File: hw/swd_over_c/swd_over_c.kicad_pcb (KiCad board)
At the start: 4 copper layers, 18.5 x 16 mm, 17 parts, among them J1 USB-C Receptacle, J2 Conn_ARM_JTAG_SWD_10, P1 USB_C_Plug, U1 ATtiny24-20M

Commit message: v1.5
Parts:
- P1: footprint alvarop:MOLEX_1054440011 -> alvarop:MOLEX_1054440011_PCBWAY
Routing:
- net GND: track 20.6 -> 20.1 mm
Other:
- board text added: "v1.5"
- board text removed: "v1.4"

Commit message: v1.6 changes
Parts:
- J1: value USB-C Receptacle -> USB_C_Receptacle_USB2.0
- P1: footprint alvarop:MOLEX_1054440011_PCBWAY -> alvarop:‎USB4155-03-C‎
- moved REF** 0.50 mm to (176.6, 67.6)
- moved P1 0.07 mm to (180.0, 67.5), turned to 90 degrees
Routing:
- net /NRST: track 15.6 -> 13.6 mm
- net /D-: track 24.3 -> 22.2 mm
- net /CC1: track 11.7 -> 9.65 mm
- net /SBU1: track 16.1 -> 14.1 mm
- net /D+: track 25.8 -> 23.8 mm
- net /SWO: track 14.3 -> 12.3 mm
- net /SHIELD: track 19.5 -> 17.9 mm
- net GND: track 20.1 -> 18.6 mm, vias 12 -> 14
- net /SBU2: track 16.2 -> 15.8 mm, vias 1 -> 2
- net /SWDCLK: track 14.0 -> 13.7 mm, vias 0 -> 1
- net /SWDIO: track 14.1 -> 13.8 mm, vias 0 -> 1
- net VBUS: track 8.53 -> 8.37 mm, vias 5 -> 7
- net /CC2: track 12.5 -> 12.6 mm, vias 1 -> 2
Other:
- board size 18.5 x 16 mm -> 25 x 16 mm
- board text added: "v1.6"
- board text removed: "v1.5"

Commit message: Somehow got the values for R4 and R5 swapped...
Swapped them in schematic and in code (manually reworked v1.6 boards to swap R4/R5)
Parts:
- R4: value 56k -> 10k
- R5: value 10k -> 56k
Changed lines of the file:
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@@
   (title_block
     (title "Debugotron - SWD to USB-C")
-    (date "2022-05-15")
-    (rev "1.6")
+    (date "2022-06-07")
+    (rev "1.7")
     (company "Quesadillon LLC")
   )
@@
     (descr "Resistor SMD 0402 (1005 Metric), square (rectangular) end terminal, IPC_7351 nominal, (Body size source: IPC-SM-782 page 72, https://www.pcb-3d.com/wordpress/wp-content/uploads/ipc-sm-782a_amendment_1_and_2.pdf), generated with kicad-footprint-generator")
     (tags "resistor")
-    (property "Description" "RES 56K OHM 1% 1/16W 0402")
+    (property "Description" "RES 10K OHM 1% 1/16W 0402")
     (property "Footprint(Generic)" "R0402")
-    (property "MPN" "RC0402FR-0756KL")
+    (property "MPN" "RC0402FR-0710KL")
     (property "Manufacturer" "Yageo")
     (property "Sheetfile" "swd_over_c.kicad_sch")
     (property "Sheetname" "")
     (property "Vendor" "Digi-Key")
-    (property "Vendor Part Number" "311-56.0KLRCT-ND")
+    (property "Vendor Part Number" "311-10.0KLRCT-ND")
     (attr smd)
     (fp_text reference "R4" (at 0 -1.17) (layer "F.SilkS") hide
       (effects (font (size 1 1) (thickness 0.15)))
     )
-    (fp_text value "56k" (at -2.074995 0.30001) (layer "F.Fab") hide
+    (fp_text value "10k" (at -2.074995 0.30001) (layer "F.Fab") hide
       (effects (font (size 1 1) (thickness 0.15)))
     )
@@
   (footprint "alvarop:‎USB4155-03-C‎" (layer "F.Cu")
     (at 179.999996 67.499992 90)
-    (property "Description" "CONN PLUG USB3.1 TYPEC BRD EDGE")
-    (property "Footprint(Generic)" "1054440011")
-    (property "MPN" "1054440011")
-    (property "Manufacturer" "Molex")
-    (property "Sheetfile" "swd_over_c.kicad_sch")
-    (property "Sheetname" "")
-    (property "Vendor" "Digi-Key")
-    (property "Vendor Part Number" "900-1054440011CT-ND")
+    (property "Description" "USB TYPE C, PLUG, SMT , G/F, RIG")
+    (property "Footprint(Generic)" "USB4155-03-C")
+    (property "MPN" "USB4155-03-C")
+    (property "Manufacturer" "GCT")
+    (property "Sheetfile" "swd_over_c.kicad_sch")
+    (property "Sheetname" "")
+    (property "Vendor" "Digi-Key")
+    (property "Vendor Part Number" "2073-USB4155-03-CCT-ND")
     (attr smd)
     (fp_text reference "P1" (at 0.125 -4.8 90 unlocked) (layer "F.SilkS") hide
@@
     (descr "Resistor SMD 0402 (1005 Metric), square (rectangular) end terminal, IPC_7351 nominal, (Body size source: IPC-SM-782 page 72, https://www.pcb-3d.com/wordpress/wp-content/uploads/ipc-sm-782a_amendment_1_and_2.pdf), generated with kicad-footprint-generator")
     (tags "resistor")
-    (property "Description" "RES 10K OHM 1% 1/16W 0402")
+    (property "Description" "RES 56K OHM 1% 1/16W 0402")
     (property "Footprint(Generic)" "R0402")
-    (property "MPN" "RC0402FR-0710KL")
+    (property "MPN" "RC0402FR-0756KL")
     (property "Manufacturer" "Yageo")
     (property "Sheetfile" "swd_over_c.kicad_sch")
     (property "Sheetname" "")
     (property "Vendor" "Digi-Key")
-    (property "Vendor Part Number" "311-10.0KLRCT-ND")
+    (property "Vendor Part Number" "311-56.0KLRCT-ND")
     (attr smd)
     (fp_text reference "R5" (at 0 -1.17) (layer "F.SilkS") hide
       (effects (font (size 1 1) (thickness 0.15)))
     )
-    (fp_text value "10k" (at 0.260009 1.149993) (layer "F.Fab") hide
-      (effects (font (size 1 1) (thickness 0.15)))
-    )
+    (fp_text value "56k" (at 0.260009 1.149993) (layer "F.Fab") hide
+      (effects (font (size 1 1) (thickness 0.15)))
+    )

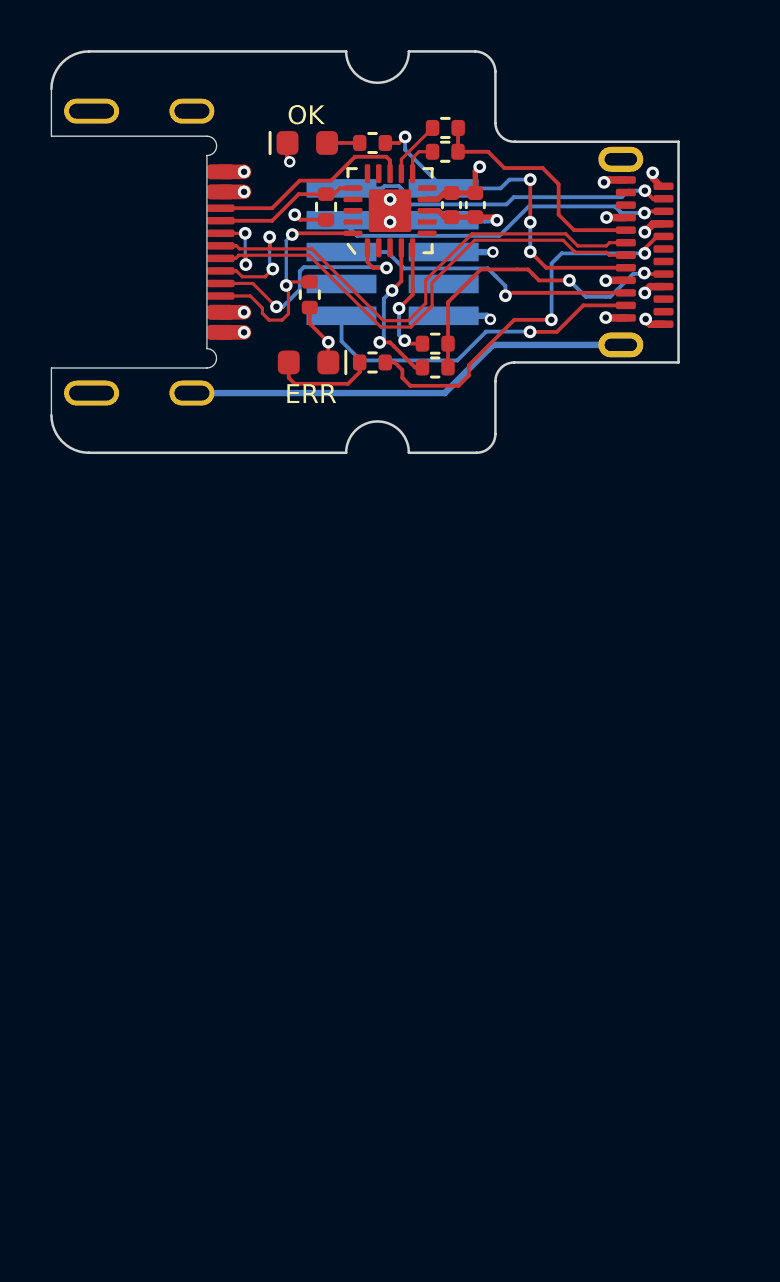
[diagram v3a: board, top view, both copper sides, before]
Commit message: v2.0 SWD Over C
Going to a different MCU since it's available at JLC and both USB-C connectors instead of plugs.
_maybe_ this will work with a short USBC cable with all the conductors and make things much easier
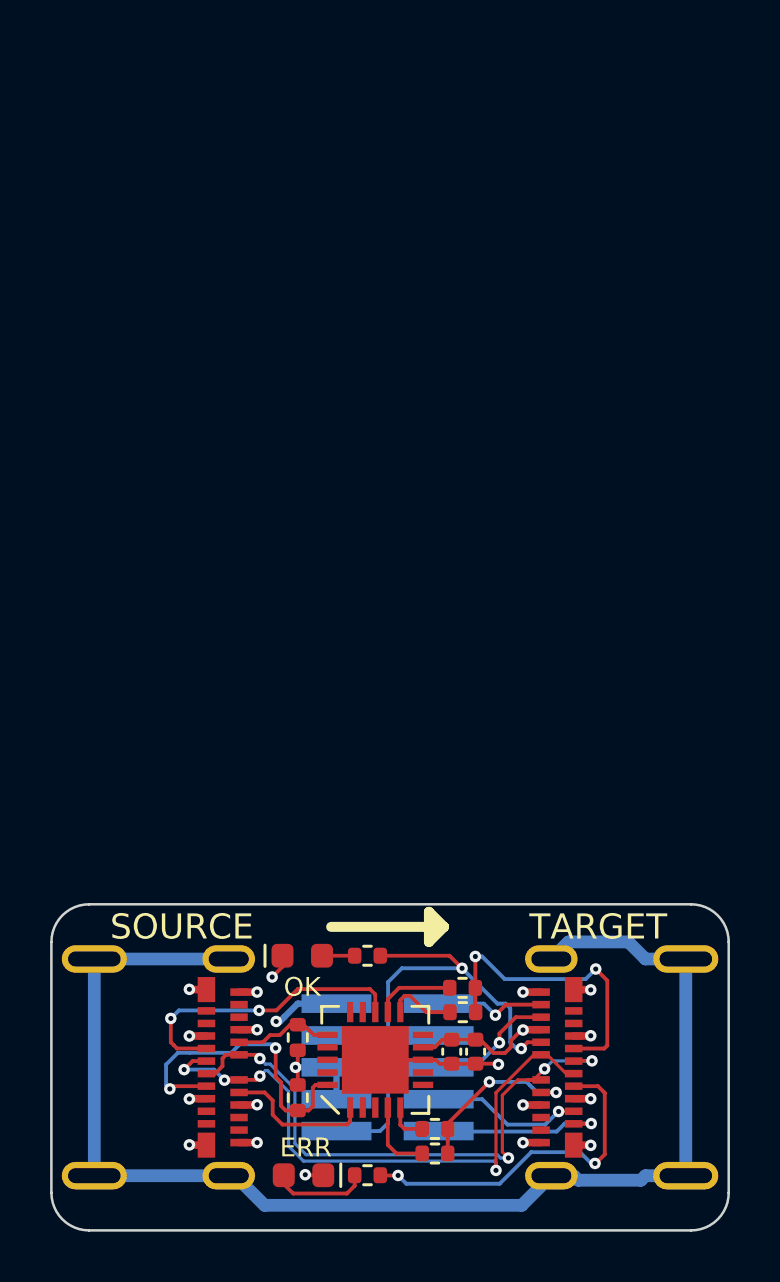
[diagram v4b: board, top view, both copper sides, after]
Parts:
- removed P1: USB_C_Plug, alvarop:‎USB4155-03-C‎
- added J3: USB_C_Receptacle, alvarop:MOLEX-1054500101, F.Cu at (174.9, 100.0)
- J1: value USB_C_Receptacle_USB2.0 -> USB_C_Receptacle; footprint alvarop:USB4500-03 -> alvarop:MOLEX-1054500101
- U1: footprint ultralibrarian:ATTINY24A-MMH_MOD -> ultralibrarian:ATTINY24A-MU
- moved R4 40.9 mm to (170.3, 103.4)
- moved R3 39.0 mm to (170.3, 102.5)
- moved U1 33.9 mm to (167.9, 99.7)
- moved C1 33.8 mm to (171.0, 99.4)
- moved C2 33.8 mm to (171.9, 99.4)
- moved R2 33.1 mm to (164.8, 98.8)
- moved J1 32.5 mm to (162.1, 100.0)
- moved J2 32.5 mm to (168.4, 100.0), turned to 90 degrees
- moved D1 32.4 mm to (165.0, 95.5)
- moved R7 32.4 mm to (167.6, 95.5)
- moved D2 32.4 mm to (165.1, 104.3)
- moved R8 32.4 mm to (167.6, 104.3)
- moved REF** 32.4 mm to (176.6, 100.0)
- moved R1 32.0 mm to (164.8, 101.2), turned to -90 degrees
- moved R6 26.7 mm to (171.4, 97.8)
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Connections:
- U1 pad 11: /CC1_R1 -> /CC2_R2
- U1 pad 12: /CC1_R2 -> /CC2_R1
- U1 pad 4: /CC2_R1 -> /CC1_R2
- U1 pad 5: /CC2_R2 -> /CC1_R1
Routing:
- net /SHIELD: track 17.9 -> 53.3 mm
- net /NRST: track 13.6 -> 4.45 mm
- net /SWDCLK: track 13.7 -> 6.01 mm
- net /SWO: track 12.3 -> 5.13 mm
- net /SWDIO: track 13.8 -> 6.93 mm
- net /SBU1: track 14.1 -> 19.8 mm, vias 4 -> 2
- net /MCURST: track 8.18 -> 11.9 mm, vias 0 -> 2
- net /SCK: track 9.52 -> 5.89 mm, vias 2 -> 0
- net /CC2_R1: track 6.25 -> 3.17 mm, vias 2 -> 0
- net /CC1: track 9.65 -> 6.99 mm, vias 0 -> 2
- net /CC2_IN_MISO: track 10.1 -> 12.5 mm
- net VBUS: track 8.37 -> 10.5 mm, vias 7 -> 8
- net /SBU2: track 15.8 -> 13.8 mm
- net /CC2_R2: track 4.78 -> 2.79 mm, vias 2 -> 0
- net /CC1_IN_MOSI: track 5.81 -> 3.98 mm
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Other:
- board size 25 x 16 mm -> 27 x 13 mm
- board text added: "SOURCE"
- board text added: "TARGET"
- board text added: "v2.0"
- board text removed: "Leave room for USB-C plug here!"
- board text removed: "v1.6"
